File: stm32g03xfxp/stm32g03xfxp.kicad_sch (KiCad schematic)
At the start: 17 parts, among them J1 USB2.0_C_v3, J3 ProMicro-RightPin, SW1 SW_Push, U2 AMS1117-3.3, U2 STM32G030F6P6

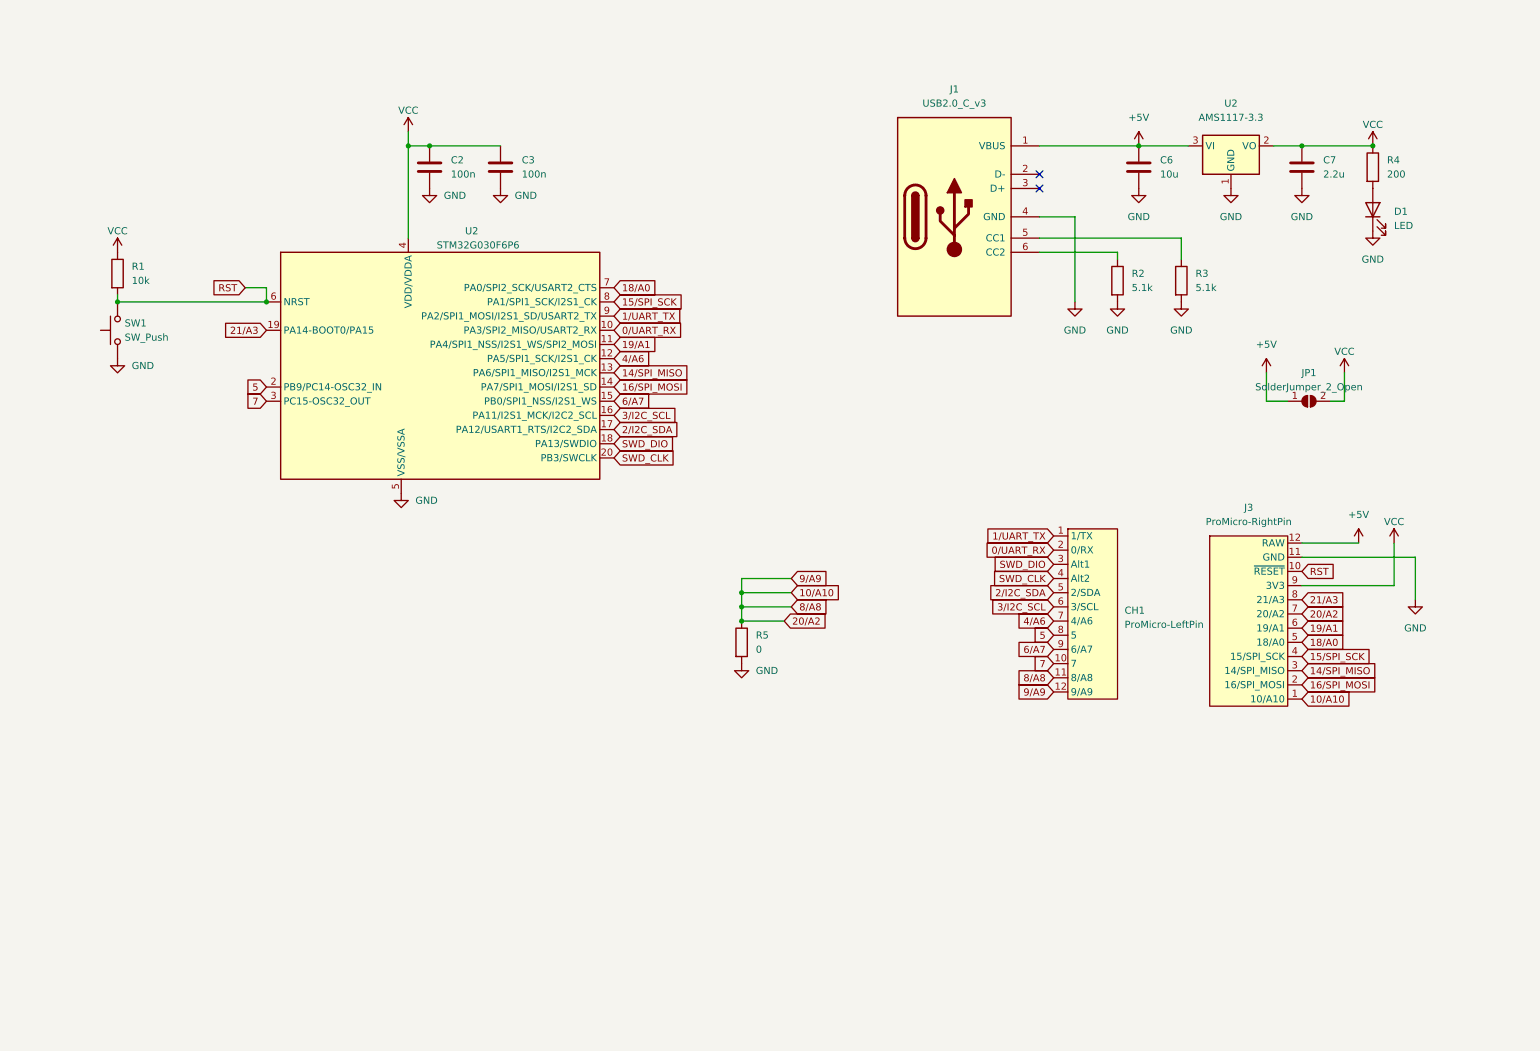
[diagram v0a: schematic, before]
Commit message: fix dio/clk
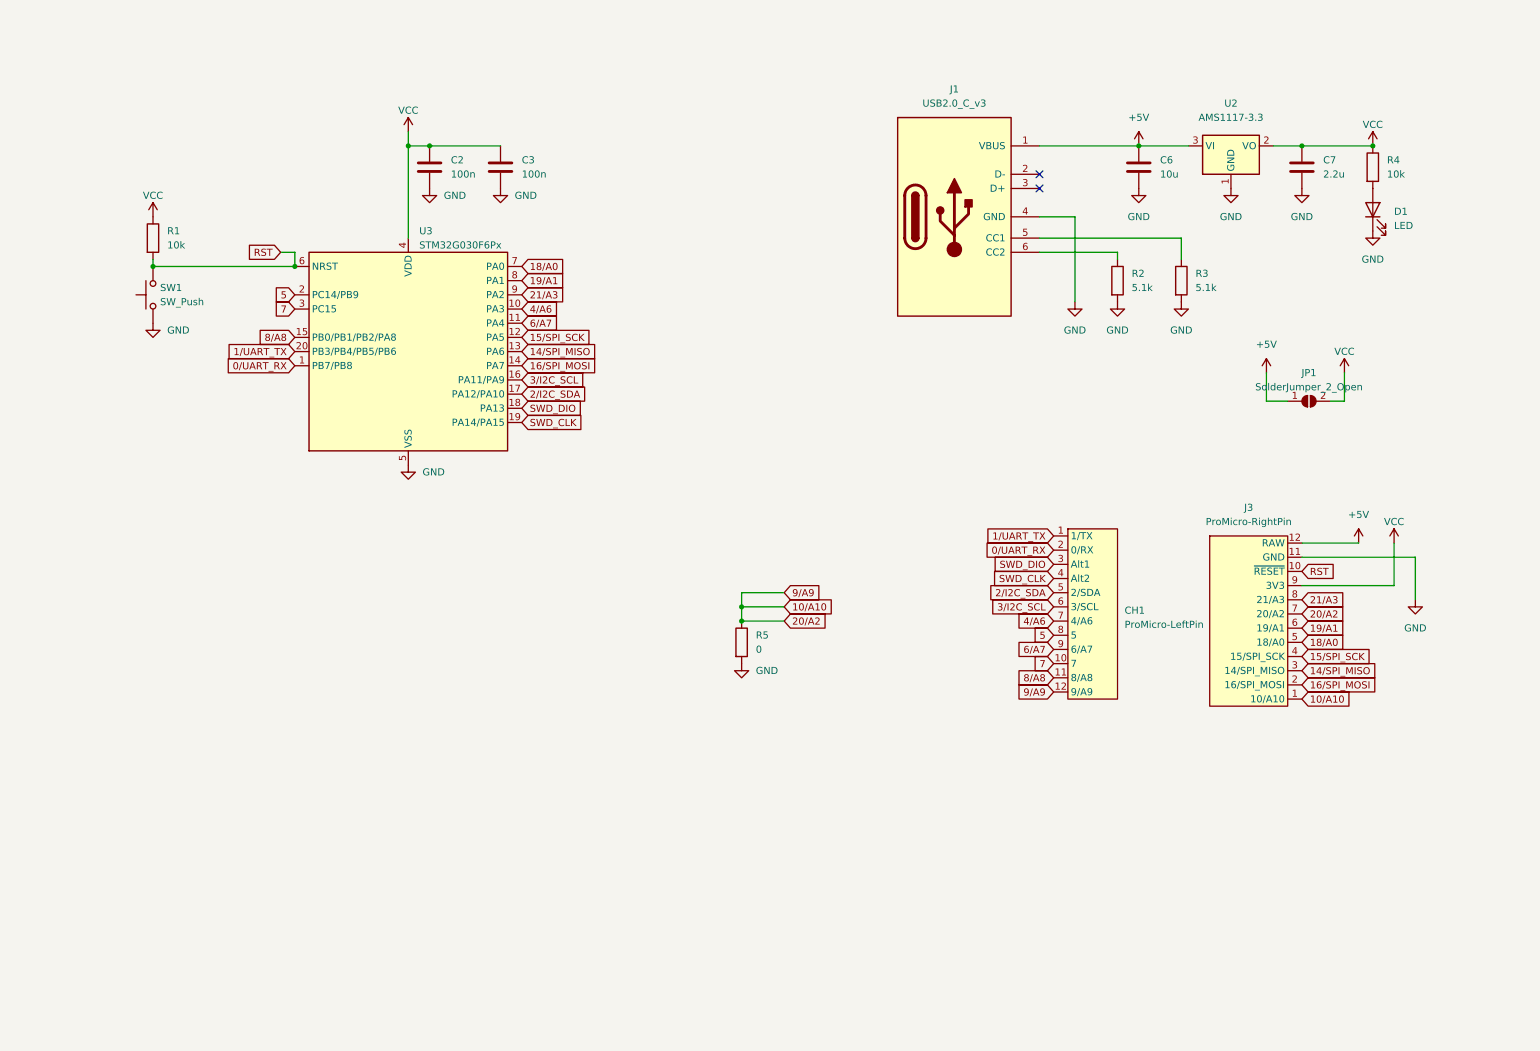
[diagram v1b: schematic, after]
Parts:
- removed U2: STM32G030F6P6, Package_SO:TSSOP-20_4.4x6.5mm_P0.65mm, symbol $74th:STM32G030F6P6
- added U3: STM32G030F6Px, Package_SO:TSSOP-20_4.4x6.5mm_P0.65mm, symbol MCU_ST_STM32G0:STM32G030F6Px
- R4: value 200 -> 10k
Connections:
- net 0/UART_RX: now also U3.1 (PB7/PB8)
- net 10/A10: no longer CH1.11 (8/A8)
- net 14/SPI_MISO: now also U3.13 (PA6)
- net 15/SPI_SCK: now also U3.12 (PA5)
- net 16/SPI_MOSI: now also U3.14 (PA7)
- net 18/A0: now also U3.7 (PA0)
- net 19/A1: now also U3.8 (PA1)
- net 1/UART_TX: now also U3.20 (PB3/PB4/PB5/PB6)
- net 21/A3: now also U3.9 (PA2)
- net 2/I2C_SDA: now also U3.17 (PA12/PA10)
- net 3/I2C_SCL: now also U3.16 (PA11/PA9)
- net 4/A6: now also U3.10 (PA3)
- net 5: now also U3.2 (PC14/PB9)
- net 6/A7: now also U3.11 (PA4)
- net 7: now also U3.3 (PC15)
- net GND: now also U3.5 (VSS)
- net RST: now also U3.6 (NRST)
- net SWD_CLK: now also U3.19 (PA14/PA15)
- net SWD_DIO: now also U3.18 (PA13)
- net VCC: now also U3.4 (VDD)
- new net 8/A8: CH1.11 (8/A8), U3.15 (PB0/PB1/PB2/PA8)
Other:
- moved on the sheet: R1, SW1

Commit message: v1.1.1
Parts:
- D1: value LED -> Blue
- renumbered U3 to U2
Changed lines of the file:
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@@
       (project "stm32g03xfxp"
         (path "/ad8c6d77-a94b-49d3-bd09-1716910d0c7d"
-          (reference "R5") (unit 1)
+          (reference "R4") (unit 1)
         )
       )
@@
   (symbol (lib_id "MCU_ST_STM32G0:STM32G030F6Px") (at 83.82 73.66 0) (unit 1)
     (in_bom yes) (on_board yes) (dnp no) (fields_autoplaced)
-    (property "Reference" "U3" (at 85.7759 52.07 0)
+    (property "Reference" "U2" (at 85.7759 52.07 0)
       (effects (font (size 1.27 1.27)) (justify left))
     )
@@
       (project "stm32g03xfxp"
         (path "/ad8c6d77-a94b-49d3-bd09-1716910d0c7d"
-          (reference "U3") (unit 1)
+          (reference "U2") (unit 1)
         )
       )
@@
       (project "stm32g03xfxp"
         (path "/ad8c6d77-a94b-49d3-bd09-1716910d0c7d"
-          (reference "R4") (unit 1)
+          (reference "R5") (unit 1)
         )
       )
@@
       (project "stm32g03xfxp"
         (path "/ad8c6d77-a94b-49d3-bd09-1716910d0c7d"
-          (reference "R2") (unit 1)
+          (reference "R1") (unit 1)
         )
       )
@@
       (project "stm32g03xfxp"
         (path "/ad8c6d77-a94b-49d3-bd09-1716910d0c7d"
-          (reference "J3") (unit 1)
+          (reference "J2") (unit 1)
         )
       )
@@
       (project "stm32g03xfxp"
         (path "/ad8c6d77-a94b-49d3-bd09-1716910d0c7d"
-          (reference "R3") (unit 1)
+          (reference "R2") (unit 1)
         )
       )
@@
   (symbol (lib_id "Device:LED") (at 256.54 48.26 90) (unit 1)
     (in_bom yes) (on_board yes) (dnp no) (fields_autoplaced)
-    (property "Reference" "D1" (at 260.35 48.5774 90)
+    (property "Reference" "D1" (at 260.35 49.2125 90)
       (effects (font (size 1.27 1.27)) (justify right))
     )
-    (property "Value" "LED" (at 260.35 51.1174 90)
+    (property "Value" "Blue" (at 260.35 51.7525 90)
       (effects (font (size 1.27 1.27)) (justify right))
     )
@@
       (project "stm32g03xfxp"
         (path "/ad8c6d77-a94b-49d3-bd09-1716910d0c7d"
-          (reference "R1") (unit 1)
-        )
-      )
+          (reference "R3") (unit 1)
+        )
+      )

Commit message: v1.2.0
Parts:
- removed JP1: SolderJumper_2_Open, Jumper:SolderJumper-2_P1.3mm_Open_RoundedPad1.0x1.5mm, symbol Jumper:SolderJumper_2_Open
- added J3: DAPLink-SWD-Recv-6Pin, $74th:BoxPinHeader_2x03_P1.27mm_Vertical, symbol $74th:DAPLink-SWD-Recv-6Pin
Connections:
- net +5V: now also J3.2 (VCC)
- net 0/UART_RX: now also J3.5 (RXD)
- net 1/UART_TX: now also J3.3 (TXD)
- net GND: now also J3.4 (GND)
- net SWD_CLK: now also J3.6 (SWCLK)
- net SWD_DIO: now also J3.1 (SWDIO)
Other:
- moved on the sheet: CH1, J3, R5

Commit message: update README
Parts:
- renumbered J3 to CH3
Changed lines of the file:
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@@
   (symbol (lib_id "$74th:DAPLink-SWD-Recv-6Pin") (at 228.6 144.78 0) (unit 1)
     (in_bom yes) (on_board yes) (dnp no) (fields_autoplaced)
-    (property "Reference" "J3" (at 228.6 137.16 0)
+    (property "Reference" "CH3" (at 228.6 137.16 0)
       (effects (font (size 1.27 1.27)))
     )
@@
       (project "stm32g03xfxp"
         (path "/ad8c6d77-a94b-49d3-bd09-1716910d0c7d"
-          (reference "J3") (unit 1)
+          (reference "CH3") (unit 1)
         )
       )
@@
       (project "stm32g03xfxp"
         (path "/ad8c6d77-a94b-49d3-bd09-1716910d0c7d"
-          (reference "J2") (unit 1)
+          (reference "CH2") (unit 1)
         )
       )
@@
   )
   (symbol (lib_id "$74th:ProMicro-LeftPin-NoGND") (at 201.93 106.68 0) (unit 1)
-    (in_bom yes) (on_board yes) (dnp no) (fields_autoplaced)
-    (property "Reference" "CH1" (at 208.28 109.855 0)
-      (effects (font (size 1.27 1.27)) (justify left))
-    )
-    (property "Value" "ProMicro-LeftPin" (at 208.28 112.395 0)
-      (effects (font (size 1.27 1.27)) (justify left))
-    )
+    (in_bom yes) (on_board yes) (dnp no)
+    (property "Reference" "CH1" (at 199.39 91.44 0)
+      (effects (font (size 1.27 1.27)) (justify left))
+    )
+    (property "Value" "ProMicro-LeftPin" (at 193.04 93.98 0)
+      (effects (font (size 1.27 1.27)) (justify left))
+    )

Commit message: stm32g03xfxp/v1.2.0
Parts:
- removed CH3: DAPLink-SWD-Recv-6Pin, $74th:BoxPinHeader_2x03_P1.27mm_Vertical, symbol $74th:DAPLink-SWD-Recv-6Pin
- removed R5: 0, $74th:Register_0805_2012, symbol Device:R
- added J2: SWD-MCU_Side-10Pin, $74th:SWD_2x05_P1.27mm, symbol $74th:SWD-MCU_Side-10Pin
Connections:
- net 10/A10 is gone; now on net GND: CH1.12 (9/A9), J3.1 (10/A10), J3.7 (20/A2)
- net 0/UART_RX: now also J2.7 (RXD)
- net 18/A0: now also U2.10 (PA3); no longer U2.7 (PA0)
- net 19/A1: now also U2.11 (PA4); no longer U2.8 (PA1)
- net 1/UART_TX: now also J2.8 (TXD)
- net 21/A3: now also U2.15 (PB0/PB1/PB2/PA8); no longer U2.9 (PA2)
- net 4/A6: now also U2.2 (PC14/PB9); no longer U2.10 (PA3)
- net 5: now also U2.3 (PC15); no longer U2.2 (PC14/PB9)
- net 6/A7: now also U2.7 (PA0); no longer U2.11 (PA4)
- net 7: now also U2.8 (PA1); no longer U2.3 (PC15)
- net 8/A8: now also U2.9 (PA2); no longer U2.15 (PB0/PB1/PB2/PA8)
- net GND: now also J2.3 (GND), J2.5 (GND), J2.9 (GND)
- net RST: now also J2.10 (~{RESET})
- net 14/SPI_MISO renamed 14/API_MISO
- net SWD_CLK renamed SWCLK
- net SWCLK: now also J2.4 (SWCLK)
- net SWD_DIO renamed SWDIO
- net SWDIO: now also J2.2 (SWDIO)
- net VCC renamed +3V3
- net +3V3: now also J2.1 (VCC)
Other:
- note added: "Alternate Pin"
- note added: "MCU"
- note added: "Pin Header"
- note added: "SWD"
- note added: "USB Power"

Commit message: update metadata
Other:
- title: (none) -> STM32G03xFxP ProMicro
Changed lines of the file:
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@@
 (kicad_sch (version 20230121) (generator eeschema)
   (paper "A4")
+  (title_block
+    (title "STM32G03xFxP ProMicro")
+    (rev "1.3.0")
+  )
   (junction (at 95.25 156.21) (diameter 0) (color 0 0 0 0)
   )
